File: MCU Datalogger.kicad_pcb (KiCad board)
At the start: 2 copper layers, 29 parts, among them J1 Conn_01x09_Pin, J2 Conn_02x03_Odd_Even, U1 24LC1025, U2 24LC1025, U3 DS1337S_, U4 ATMEGA328P-AU, Y1 32.768 KHz, Y2 16 MHz

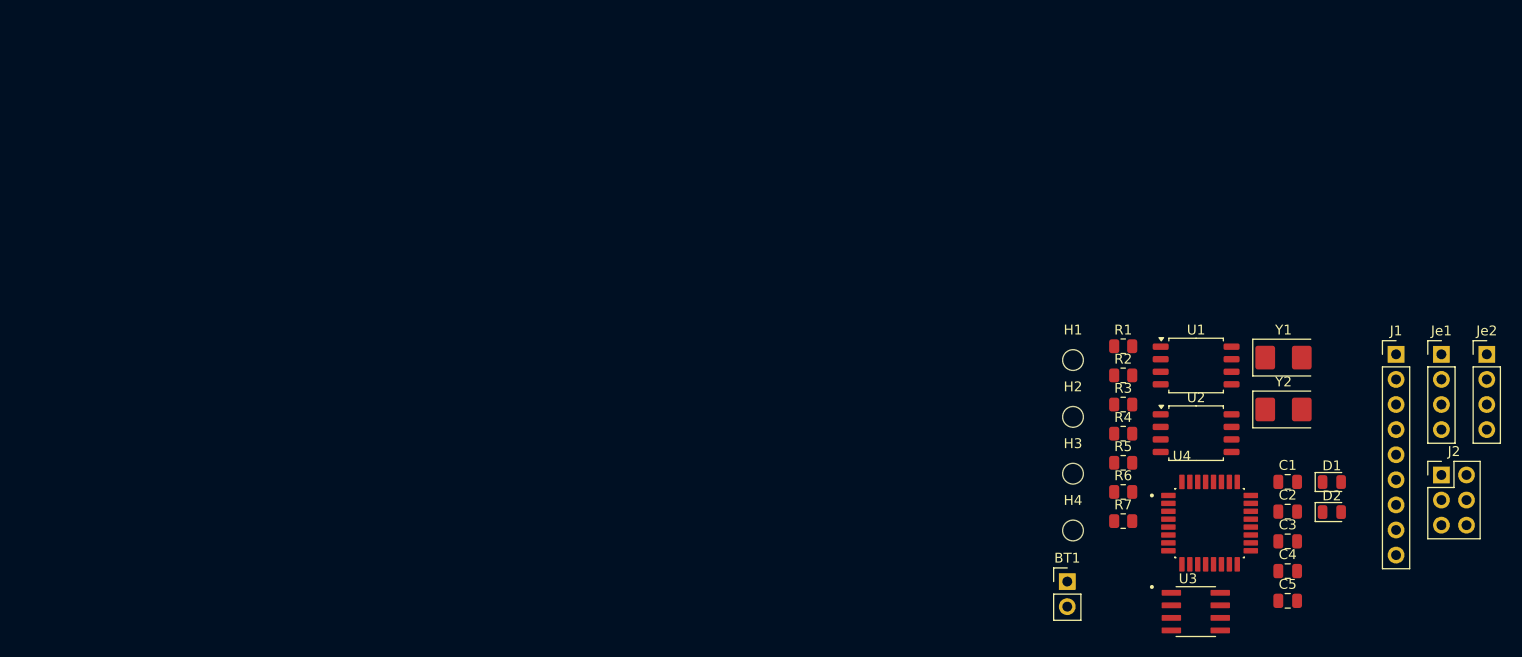
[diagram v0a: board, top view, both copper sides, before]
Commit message: adding footprints for PCBnew with arrangment.
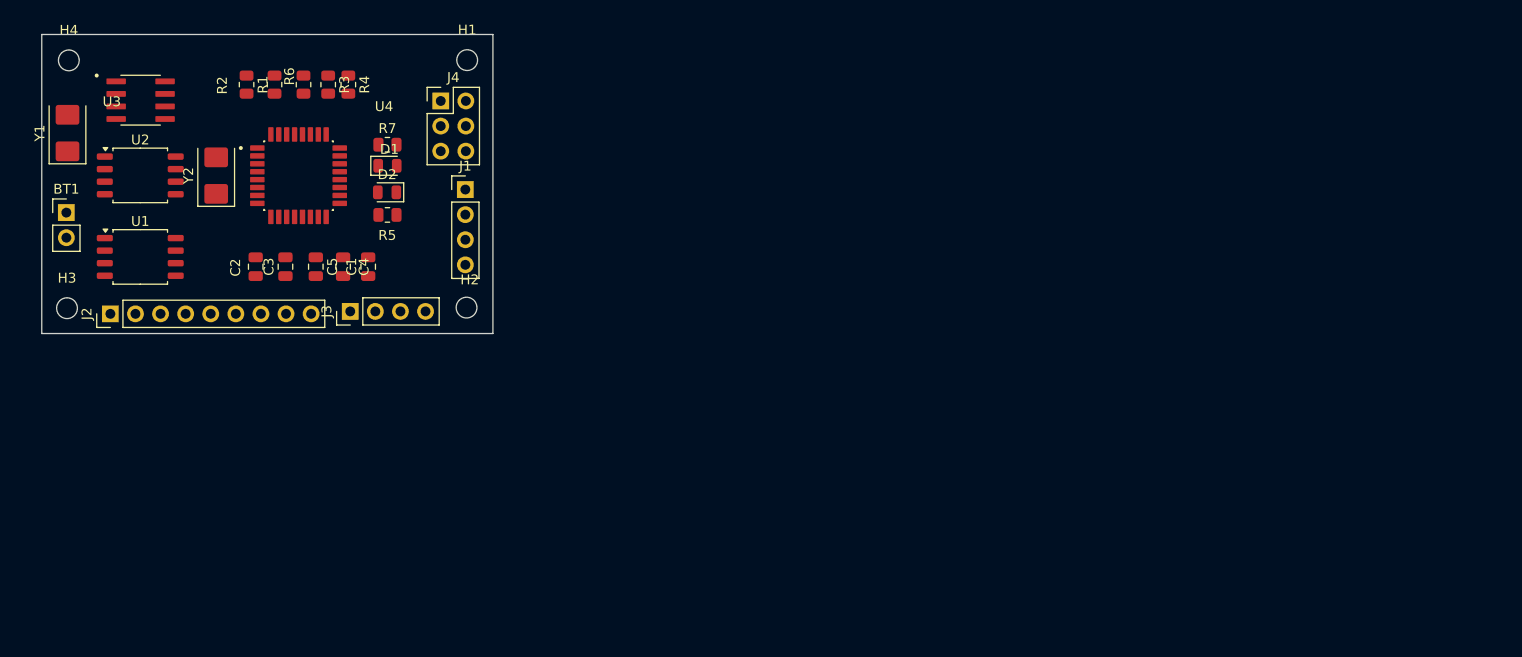
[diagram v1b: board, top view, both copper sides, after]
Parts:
- moved J2 130.2 mm to (115.9, 109.0), turned to 90 degrees
- moved Y1 125.2 mm to (111.6, 90.7), turned to 90 degrees
- moved U3 118.7 mm to (119.0, 87.3)
- moved H4 112.2 mm to (111.7, 83.3)
- moved Y2 110.6 mm to (126.6, 95.0), turned to 90 degrees
- moved J3 110.5 mm to (140.2, 108.7), turned to 90 degrees
- moved U2 110.0 mm to (119.0, 95.0)
- moved J4 108.1 mm to (149.4, 87.4)
- moved BT1 108.0 mm to (111.5, 98.7)
- moved U1 107.4 mm to (119.0, 103.2)
- moved C2 107.4 mm to (130.6, 104.2), turned to 90 degrees
- moved C3 105.2 mm to (133.7, 104.2), turned to 90 degrees
- moved J1 104.7 mm to (151.9, 96.4)
- moved C5 104.0 mm to (136.7, 104.2), turned to -90 degrees
- moved H3 103.2 mm to (111.5, 108.4)
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- renumbered Je2 to J1, J1 to J2, Je1 to J3, J2 to J4
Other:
- board outline added: 45.7 x 30.3 mm

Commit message: Routing sans GNC VCC complete.
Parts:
- moved R2 23.3 mm to (121.7, 104.6), turned to 0 degrees
- moved C1 22.5 mm to (130.1, 85.1), turned to 0 degrees
- moved R1 22.4 mm to (117.6, 104.6), turned to 180 degrees
- moved C5 19.2 mm to (134.7, 85.1), turned to 180 degrees
- moved U1 16.2 mm to (119.5, 87.0)
- moved R6 15.1 mm to (144.7, 94.7), turned to 0 degrees
- moved U3 12.5 mm to (119.4, 99.8)
- moved D2 12.0 mm to (140.5, 85.1), turned to 0 degrees
- moved R5 11.2 mm to (140.5, 88.3), turned to 180 degrees
- moved C3 10.7 mm to (125.3, 97.5), turned to 0 degrees
- moved C2 10.1 mm to (140.4, 101.8), turned to 180 degrees
- moved Y1 9.60 mm to (112.5, 100.2)
- moved R3 9.28 mm to (140.5, 94.7), turned to 180 degrees
- moved D1 8.88 mm to (144.7, 85.1)
- moved BT1 6.58 mm to (112.2, 92.2), turned to 180 degrees
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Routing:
- net GND: track 0.00 -> 129.5 mm, vias 0 -> 5
- net /Vcc: track 0.00 -> 128.7 mm, vias 0 -> 6
- net /SCK: track 0.00 -> 94.3 mm, vias 0 -> 7
- net /SDA: track 0.00 -> 94.0 mm, vias 0 -> 6
- net Net-(BT1-+): track 0.00 -> 50.4 mm, vias 0 -> 2
- net Net-(U4-PB6): track 0.00 -> 42.0 mm
- net /D2: track 0.00 -> 32.1 mm, vias 0 -> 1
- net /TX: track 0.00 -> 29.7 mm, vias 0 -> 2
- net /RX: track 0.00 -> 27.7 mm, vias 0 -> 1
- net /D3: track 0.00 -> 26.1 mm, vias 0 -> 1
- net /D4: track 0.00 -> 22.3 mm, vias 0 -> 1
- net /MOSI: track 0.00 -> 21.8 mm, vias 0 -> 1
- net /RESET: track 0.00 -> 20.2 mm, vias 0 -> 2
- net /MISO: track 0.00 -> 18.3 mm, vias 0 -> 1
- net /D5: track 0.00 -> 15.4 mm
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- added copper zone on F.Cu, net /Vcc
- added copper zone on B.Cu, net GND
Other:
- board size 45.7 x 30.3 mm -> 50 x 33.4 mm

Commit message: finish routing with filling zones/
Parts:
- moved BT1 0.78 mm to (113.0, 92.2)
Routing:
- net /Vcc: track 128.7 -> 33.3 mm, vias 6 -> 2
- net /SCK: track 94.3 -> 115.8 mm, vias 7 -> 8
- net GND: track 129.5 -> 148.0 mm
- net Net-(U4-PB6): track 42.0 -> 25.7 mm, vias 0 -> 2
- net /SDA: track 94.0 -> 86.2 mm, vias 6 -> 8
- net Net-(BT1-+): track 50.4 -> 56.5 mm, vias 2 -> 3
- net /D2: track 32.1 -> 30.6 mm
- net /TX: track 29.7 -> 30.3 mm, vias 2 -> 1
- net /RX: track 27.7 -> 27.1 mm

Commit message: the final editing on routing.
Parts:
- moved D1 0.50 mm to (144.9, 85.6)
- moved D2 0.46 mm to (140.5, 85.6)
- moved U3 0.30 mm to (119.1, 99.9)
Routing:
- net GND: track 148.0 -> 111.0 mm, vias 5 -> 6
- net /SCK: track 115.8 -> 91.7 mm, vias 8 -> 4
- net /Vcc: track 33.3 -> 34.3 mm, vias 2 -> 0
- net Net-(D1-K): track 3.82 -> 2.99 mm

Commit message: ready to manufacturing
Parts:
- moved R2 0.73 mm to (121.8, 103.9)
- moved R1 0.69 mm to (117.7, 103.9)
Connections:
- BT1 pad 1: Net-(BT1-+) -> /Vcc
- C5 pad 1: Net-(BT1-+) -> /Vcc
- D1 pad 2: Net-(BT1-+) -> /Vcc
- U4 pad 18: Net-(BT1-+) -> /Vcc
- U4 pad 4: Net-(BT1-+) -> /Vcc
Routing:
- net /Vcc: track 34.3 -> 91.2 mm, vias 0 -> 3
- net Net-(BT1-+): track 56.7 -> 0.00 mm, vias 3 -> 0
- net /D6: track 14.0 -> 12.7 mm
- net /D7: track 13.1 -> 11.8 mm
- net /D5: track 15.4 -> 14.2 mm
- net /D8: track 12.0 -> 11.0 mm
- net Net-(U4-PB6): track 25.7 -> 26.5 mm
- net Net-(U3-SQW/~INT): track 6.72 -> 5.96 mm
- net /SDA: track 86.5 -> 87.2 mm
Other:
- board text added: "2"
- board text added: "3"
- board text added: "4"
- board text added: "5"
- board text added: "6"
- board text added: "7"
- board text added: "8"
- board text added: "GND"
- board text added: "GPIO"
- board text added: "I2C"
- board text added: "ICSP"
- board text added: "ICSP MISO |VCC SCK |MOSI RESET|GND"
- board text added: "RX"
- board text added: "SCK"
- board text added: "SDA"
- board text added: "SERIAL"
- board text added: "TX"
- board text added: "VCC"

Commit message: adding the 3D modeles for components.
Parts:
- added REF**: KiCad-Logo2_6mm_SilkScreen, Symbol:KiCad-Logo2_6mm_SilkScreen, B.Cu at (122.2, 87.9)
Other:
- board text added: "v1.0 2 Layers desgin"

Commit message: added the gerber files.
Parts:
- moved R6 2.03 mm to (144.9, 92.7)
- moved R3 0.63 mm to (140.5, 95.3)
- moved C5 0.48 mm to (134.7, 85.6)
- moved C1 0.47 mm to (130.1, 85.6)
- moved R7 0.26 mm to (144.9, 88.2)
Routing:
- net /Vcc: track 91.2 -> 17.5 mm, vias 3 -> 0
- net /SCK: track 91.2 -> 95.7 mm
- net /SDA: track 87.2 -> 90.8 mm
- net GND: track 110.7 -> 112.4 mm
- net Net-(U4-AREF): track 9.77 -> 11.1 mm, vias 0 -> 2
- net /MISO: track 18.4 -> 19.5 mm
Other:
- board size 50 x 33.4 mm -> 48.6 x 32 mm

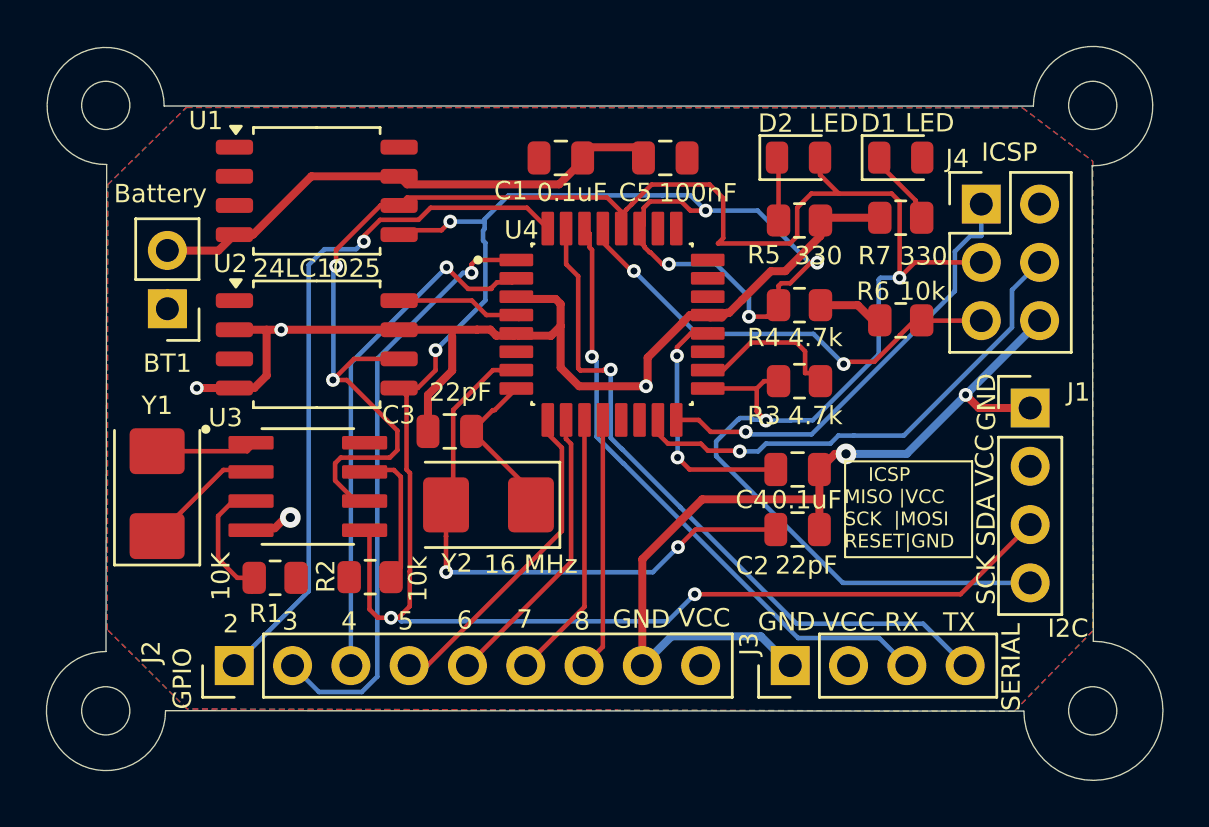
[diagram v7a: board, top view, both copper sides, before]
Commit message: completed 4Layer PCB routing.
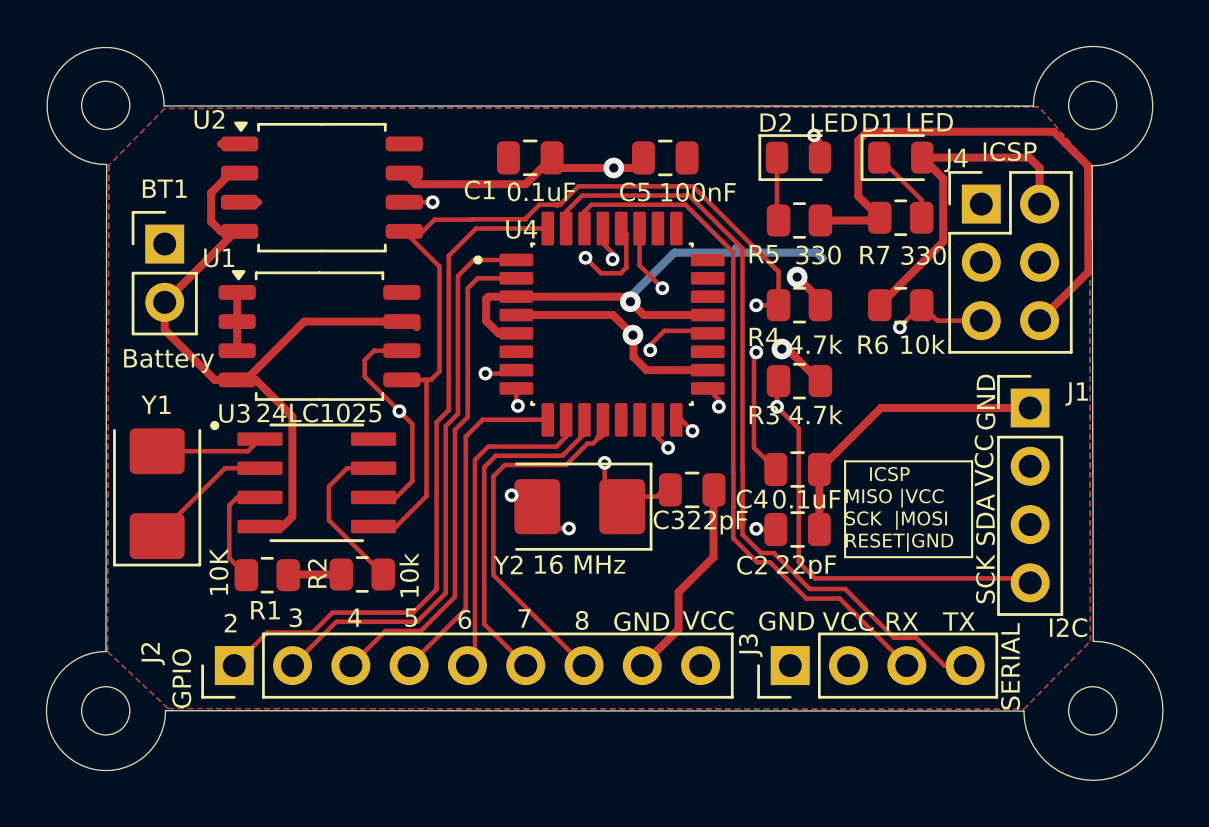
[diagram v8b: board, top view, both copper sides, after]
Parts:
- moved C3 10.9 mm to (135.8, 100.1), turned to 180 degrees
- moved U2 6.83 mm to (119.7, 86.9)
- moved U1 6.33 mm to (119.6, 93.4)
- moved Y2 3.98 mm to (130.9, 100.8)
- moved BT1 2.82 mm to (112.9, 89.4), turned to 0 degrees
- moved C1 1.34 mm to (128.8, 85.6)
- moved R6 0.66 mm to (144.9, 92.0)
- moved U3 0.42 mm to (119.5, 99.8)
- moved R1 0.36 mm to (117.3, 103.8)
- moved R2 0.36 mm to (121.5, 103.8)
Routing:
- net /Vcc: track 17.5 -> 52.1 mm, vias 0 -> 3
- net /SDA: track 90.8 -> 69.2 mm, vias 8 -> 2
- net Net-(U4-PB6): track 26.5 -> 19.3 mm, vias 2 -> 4
- net /D8: track 11.0 -> 16.6 mm
- net /TX: track 30.3 -> 34.2 mm, vias 1 -> 0
- net /RX: track 26.9 -> 30.5 mm, vias 1 -> 0
- net Net-(U4-PB7): track 7.00 -> 10.3 mm, vias 0 -> 2
- net /D7: track 11.8 -> 15.0 mm
- net Net-(U4-AREF): track 11.1 -> 13.2 mm
- net /MOSI: track 21.9 -> 23.9 mm
- net Net-(U3-~{INTA}): track 6.44 -> 4.83 mm
- net /D6: track 12.7 -> 14.2 mm
- net /D3: track 26.4 -> 24.9 mm, vias 1 -> 0
- net Net-(U3-SQW/~INT): track 5.96 -> 7.09 mm
- net /D2: track 30.8 -> 29.7 mm, vias 1 -> 0
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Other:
- copper layers 2 -> 4
